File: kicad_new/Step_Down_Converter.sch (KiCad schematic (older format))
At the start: 11 parts

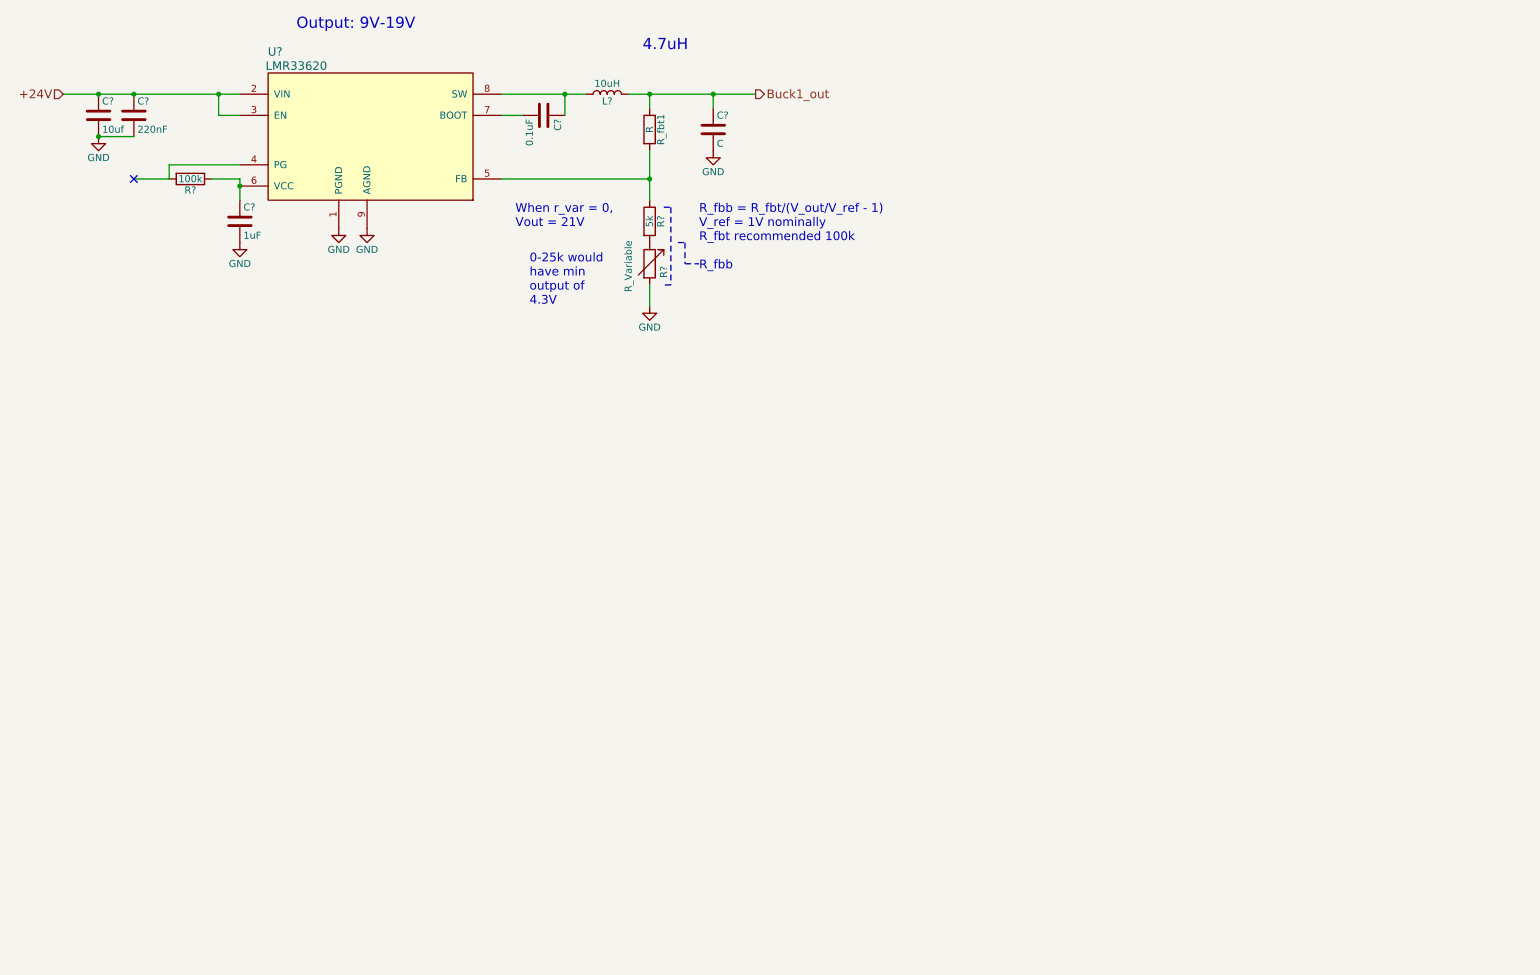
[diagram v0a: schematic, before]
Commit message: Added INA's and connectors
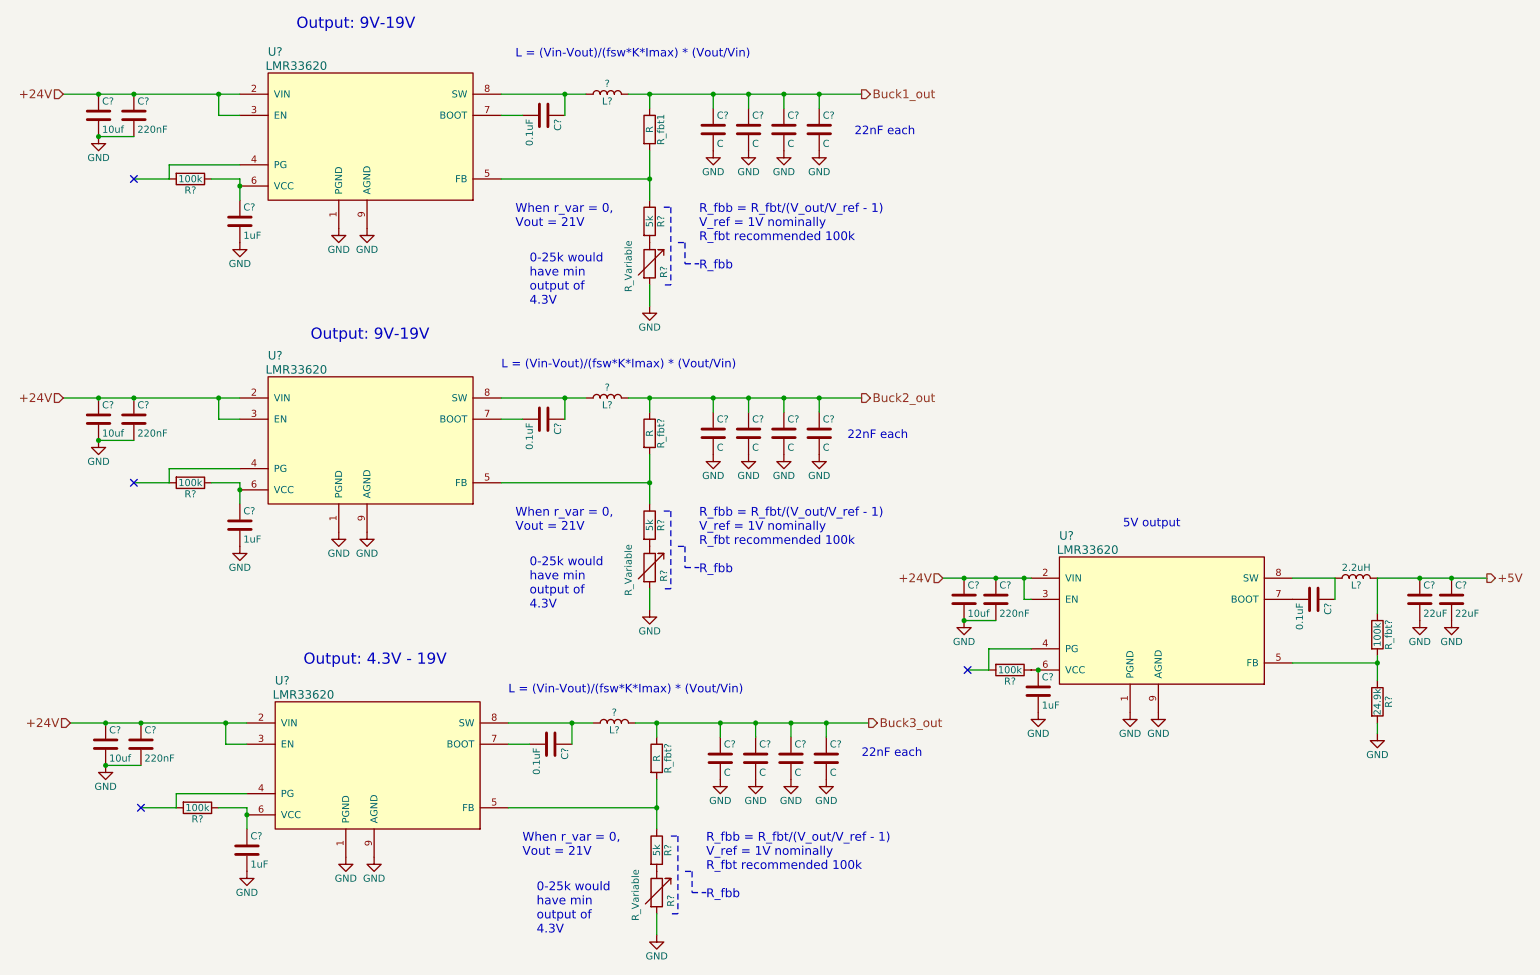
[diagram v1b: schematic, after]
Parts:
- added C? (x11): C, symbol C
- added C? (x3): 220nF, symbol C
- added C? (x3): 10uf, symbol C
- added C? (x3): 1uF, symbol C
- added C? (x3): 0.1uF, symbol C
- added C? (x2): 22uF, symbol C
- added L? (x2): ?, symbol L
- added L?: 2.2uH, symbol L
- added R? (x3), R_fbt?: 100k, symbol R
- added R? (x2): 5k, symbol R
- added R? (x2): R_Variable, symbol R_Variable
- added R?: 24.9k, symbol R
- added R_fbt? (x2): R, symbol R
- added U? (x3): LMR33620, symbol LMR33620
- L?: value 10uH -> ?
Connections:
- net +24V: now also C?.1, C?.1, C?.1, C?.1, C?.1, C?.1, U?.2 (VIN), U?.2 (VIN), U?.2 (VIN), U?.3 (EN), U?.3 (EN), U?.3 (EN)
- net Buck1_out: now also C?.1, C?.1, C?.1
- net GND: now also C?.2, C?.2, C?.2, C?.2, C?.2, C?.2, C?.2, C?.2, C?.2, C?.2, C?.2, C?.2, C?.2, C?.2, C?.2, C?.2, C?.2, C?.2, C?.2, C?.2, C?.2, C?.2, R?.2, R?.2, R?.2, U?.1 (PGND), U?.1 (PGND), U?.1 (PGND), U?.9 (AGND), U?.9 (AGND), U?.9 (AGND)
- new net: R?.2, U?.4 (PG) (x3)
- new net: R?.1, R_fbt?.2, U?.5 (FB) (x3)
- new net: C?.1, R?.1, U?.6 (VCC) (x2)
- new net: C?.2, U?.7 (BOOT) (x3)
- new net: C?.1, L?.1, U?.8 (SW) (x3)
- new net: R?.1, R?.2 (x2)
- new net: R?.1, U?.6 (VCC)
- new net +5V: C?.1, C?.1, L?.2, R_fbt?.1
- new net Buck2_out: C?.1, C?.1, C?.1, C?.1, L?.2, R_fbt?.1
- new net Buck3_out: C?.1, C?.1, C?.1, C?.1, L?.2, R_fbt?.1
- no-connect marks 1 -> 4
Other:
- note added: "22nF each"
- note added: "5V output\n"
- note added: "L = (Vin-Vout)/(fsw*K*Imax) * (Vout/Vin)"
- note added: "Output: 4.3V - 19V"
- note removed: "4.7uH"

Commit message: typo
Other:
- note added: "22uF each"
- note removed: "22nF each"
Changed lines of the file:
@@
 Output: 9V-19V
 Text Notes 6450 1700 0    60   ~ 0
-22nF each
+22uF each
 Text Notes 6400 3850 0    60   ~ 0
-22nF each
+22uF each
 Text Notes 6500 6100 0    60   ~ 0
-22nF each
+22uF each
 $Comp
 L LMR33620 U?
